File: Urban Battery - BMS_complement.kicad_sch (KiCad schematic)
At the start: 37 parts, among them J1 Conn_02x10_Odd_Even, J10 Conn_01x02_Female, J11 Conn_01x02_Female, J12 Conn_01x03, J13 Conn_01x04_Female, J2 Conn_01x02_Female, J3 Conn_01x02_Female, J4 Conn_01x02_Female, J5 Conn_01x02_Female, J6 Conn_01x03, J7 Conn_01x02_Female, J8 Conn_01x02_Female, J9 Conn_01x02_Female, K1 ADW11, K2 ADW11, SW1 Run/Charge_SW, SW2 CAN_TERM, SW3 SW_Push_LED, U1 LM2575HVS-12/NOPB, U2 MCP2515-xSO, U3 MCP2551-I-SN, Y1 8MHz

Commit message: Added temporary footprints and preliminary layout
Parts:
- removed SW1: Run/Charge_SW, symbol Switch:SW_DP3T
- added SW2: SW_DPDT_x2, BMS_Custom_Footprints:Toggle_Switch_M2022S2A2W30, symbol Switch:SW_DPDT_x2
- C1: renamed from C3; footprint (none) -> Capacitor_SMD:C_0805_2012Metric_Pad1.18x1.45mm_HandSolder
- C2: renamed from C4; footprint (none) -> Capacitor_SMD:C_0805_2012Metric_Pad1.18x1.45mm_HandSolder
- C3: renamed from C5; footprint (none) -> Capacitor_SMD:C_0805_2012Metric_Pad1.18x1.45mm_HandSolder
- C4: renamed from C6; footprint (none) -> Capacitor_SMD:C_0805_2012Metric_Pad1.18x1.45mm_HandSolder
- C6: renamed from C7; footprint (none) -> Capacitor_SMD:C_0805_2012Metric_Pad1.18x1.45mm_HandSolder
- F1: footprint (none) -> Fuse:Fuseholder_Blade_Mini_Keystone_3568
- F2: value Fuse -> 7A; footprint (none) -> Fuse:Fuseholder_Blade_Mini_Keystone_3568
- J1: value Conn_02x10_Odd_Even -> BMS IO; footprint (none) -> Connector_JST:JST_PHD_S20B-PHDSS_2x10_P2.00mm_Horizontal
- J10, J11, J9: value Conn_01x02_Female -> Thermistor; footprint (none) -> TerminalBlock_Phoenix:TerminalBlock_Phoenix_MKDS-1,5-2-5.08_1x02_P5.08mm_Horizontal
- J12: renamed from J6; value Conn_01x03 -> CAN Connector; footprint (none) -> BMS_Custom_Footprints:molex-sl-1x03-horizontal
- J13: renamed from J12; value Conn_01x03 -> CAN Connector; footprint (none) -> BMS_Custom_Footprints:molex-sl-1x03-horizontal
- J2: renamed from J13; value Conn_01x04_Female -> OLED Header; footprint (none) -> BMS_Custom_Footprints:OLED_Header
- J3, J4, J5: value Conn_01x02_Female -> E-Stop; footprint (none) -> Connector_Molex:Molex_Micro-Fit_3.0_43650-0200_1x02_P3.00mm_Horizontal
- J6: renamed from J7; value Conn_01x02_Female -> Contactor Connector; footprint (none) -> TerminalBlock_Phoenix:TerminalBlock_Phoenix_MKDS-1,5-2-5.08_1x02_P5.08mm_Horizontal
- J7: renamed from J2; value Conn_01x02_Female -> Charge Connector; footprint (none) -> Connector_Molex:Molex_Micro-Fit_3.0_43650-0200_1x02_P3.00mm_Horizontal
- J8: value Conn_01x02_Female -> Battery Connector; footprint (none) -> TerminalBlock_Phoenix:TerminalBlock_Phoenix_MKDS-1,5-2-5.08_1x02_P5.08mm_Horizontal
- K1: renamed from K2; value ADW11 -> Contactor_Relay
- K2: renamed from K1; value ADW11 -> Charge_Relay
- R1, R2, R3: footprint (none) -> Resistor_SMD:R_0805_2012Metric_Pad1.20x1.40mm_HandSolder
- Y1: footprint (none) -> Crystal:Crystal_HC49-U_Vertical
- renumbered C1 to C5, C2 to C7, SW3 to SW1, SW2 to SW3, U2 to U1, U1 to U2
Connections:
- net a2 is gone; now on net bms2: K1.6
- net a4 is gone; now on net bms4: K2.6
- net +5V: now also A1.27 (+5V), SW1.2, SW1.4 (A)
- net Buck_VIN: now also SW2.4 (A), SW2.6 (C)
- net bms2: now also SW2.1 (A)
- net bms4: now also SW2.3 (C)
- net at F1.2: now also SW2.2 (B), SW2.5 (B)
- no-connect marks 37 -> 35
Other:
- note added: "Battery Connector"
- note removed: "7A Fuse"
- note removed: "Connection to battery through bus bar pcb"
- moved on the sheet: A1, C1, C2, C3, C4, C5, C6, C7, D1, F1, F2, J1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

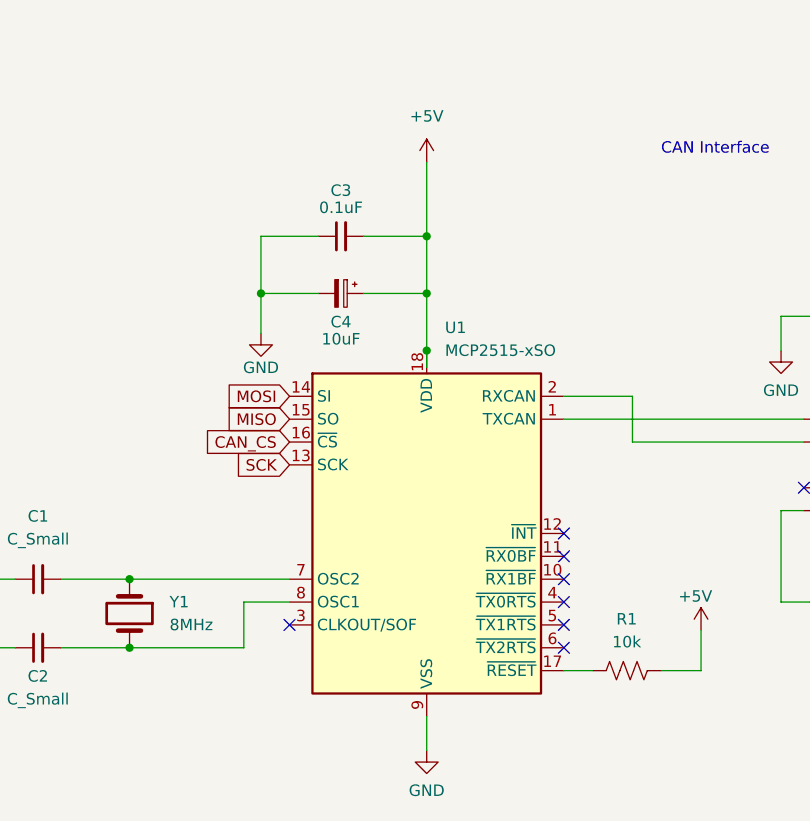
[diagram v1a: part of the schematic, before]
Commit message: Edited component placement
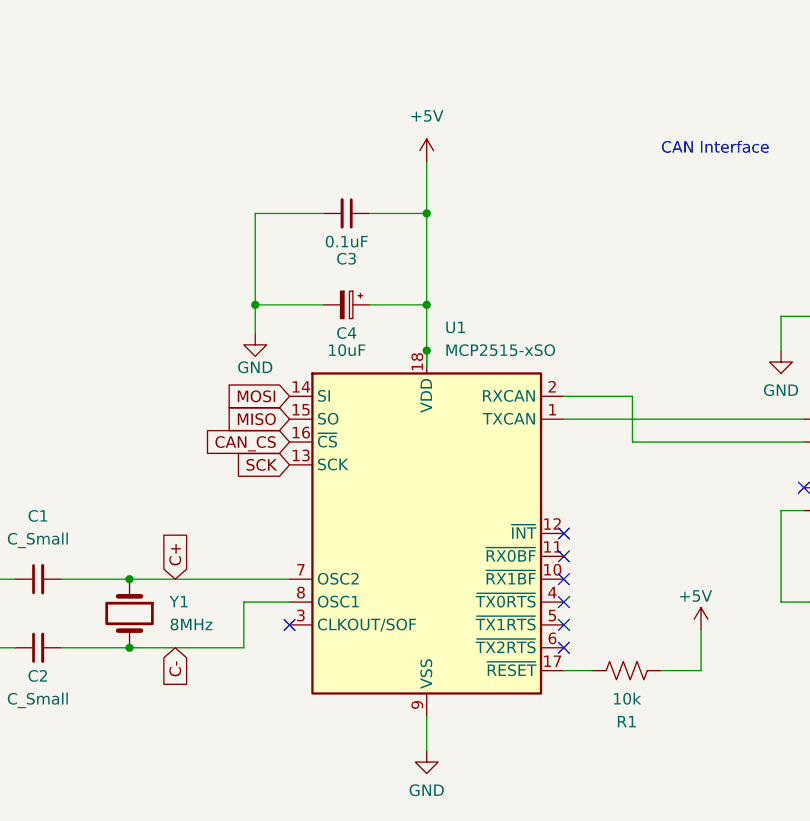
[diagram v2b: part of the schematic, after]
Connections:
- net +5V: now also C3.1, R1.1; no longer C3.2, R1.2
- net GND: now also C3.2; no longer C3.1
- net at U1.17 (~{RESET}): now also R1.2; no longer R1.1
- net C+: now reaches C1.2, U1.7 (OSC2), Y1.1
- net C-: now reaches C2.2, U1.8 (OSC1), Y1.2
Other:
- moved on the sheet: C3, C4, R1
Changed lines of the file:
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@@
   (junction (at 195.58 119.38) (diameter 0) (color 0 0 0 0)
   )
-  (junction (at 114.935 214.63) (diameter 0) (color 0 0 0 0)
-  )
   (junction (at 249.555 222.25) (diameter 0) (color 0 0 0 0)
   )
@@
   (junction (at 152.4 34.29) (diameter 0) (color 0 0 0 0)
   )
-  (junction (at 133.35 208.28) (diameter 0) (color 0 0 0 0)
-  )
   (junction (at 43.18 108.585) (diameter 0) (color 0 0 0 0)
   )
@@
   (junction (at 244.475 219.075) (diameter 0) (color 0 0 0 0)
   )
+  (junction (at 133.35 215.9) (diameter 0) (color 0 0 0 0)
+  )
   (junction (at 244.475 227.33) (diameter 0) (color 0 0 0 0)
   )
@@
   (junction (at 138.43 114.3) (diameter 0) (color 0 0 0 0)
   )
+  (junction (at 133.35 205.74) (diameter 0) (color 0 0 0 0)
+  )
   (junction (at 176.53 119.38) (diameter 0) (color 0 0 0 0)
   )
@@
   (junction (at 133.35 220.98) (diameter 0) (color 0 0 0 0)
   )
-  (junction (at 133.35 214.63) (diameter 0) (color 0 0 0 0)
-  )
   (junction (at 134.62 34.29) (diameter 0) (color 0 0 0 0)
+  )
+  (junction (at 114.3 215.9) (diameter 0) (color 0 0 0 0)
   )
   (no_connect (at 118.11 251.46))
@@
     (stroke (width 0) (type default) (color 0 0 0 0))
   )
+  (wire (pts (xy 127 205.74) (xy 133.35 205.74))
+    (stroke (width 0) (type default) (color 0 0 0 0))
+  )
   (wire (pts (xy 157.48 124.46) (xy 157.48 133.35))
     (stroke (width 0) (type default) (color 0 0 0 0))
@@
     (stroke (width 0) (type default) (color 0 0 0 0))
   )
-  (wire (pts (xy 133.35 208.28) (xy 133.35 214.63))
-    (stroke (width 0) (type default) (color 0 0 0 0))
-  )
   (wire (pts (xy 176.53 119.38) (xy 181.61 119.38))
     (stroke (width 0) (type default) (color 0 0 0 0))
@@
     (stroke (width 0) (type default) (color 0 0 0 0))
   )
-  (wire (pts (xy 121.285 208.28) (xy 114.935 208.28))
-    (stroke (width 0) (type default) (color 0 0 0 0))
-  )
   (wire (pts (xy 132.08 114.3) (xy 138.43 114.3))
     (stroke (width 0) (type default) (color 0 0 0 0))
   )
-  (wire (pts (xy 133.35 214.63) (xy 133.35 220.98))
+  (wire (pts (xy 133.35 200.025) (xy 133.35 205.74))
     (stroke (width 0) (type default) (color 0 0 0 0))
   )
@@
     (stroke (width 0) (type default) (color 0 0 0 0))
   )
+  (wire (pts (xy 114.3 215.9) (xy 114.3 219.075))
+    (stroke (width 0) (type default) (color 0 0 0 0))
+  )
   (wire (pts (xy 229.87 234.315) (xy 229.87 238.76))
     (stroke (width 0) (type default) (color 0 0 0 0))
@@
     (stroke (width 0) (type default) (color 0 0 0 0))
   )
+  (wire (pts (xy 133.35 205.74) (xy 133.35 215.9))
+    (stroke (width 0) (type default) (color 0 0 0 0))
+  )
   (wire (pts (xy 363.22 59.69) (xy 363.22 63.5))
     (stroke (width 0) (type default) (color 0 0 0 0))
@@
     (stroke (width 0) (type default) (color 0 0 0 0))
   )
-  (wire (pts (xy 133.35 200.025) (xy 133.35 208.28))
-    (stroke (width 0) (type default) (color 0 0 0 0))
-  )
-  (wire (pts (xy 126.365 214.63) (xy 133.35 214.63))
-    (stroke (width 0) (type default) (color 0 0 0 0))
-  )
   (wire (pts (xy 148.59 226.06) (xy 156.21 226.06))
     (stroke (width 0) (type default) (color 0 0 0 0))
@@
     (stroke (width 0) (type default) (color 0 0 0 0))
   )
-  (wire (pts (xy 114.935 214.63) (xy 114.935 219.075))
+  (wire (pts (xy 114.3 215.9) (xy 121.92 215.9))
     (stroke (width 0) (type default) (color 0 0 0 0))
   )
@@
     (stroke (width 0) (type default) (color 0 0 0 0))
   )
-  (wire (pts (xy 114.935 214.63) (xy 121.285 214.63))
+  (wire (pts (xy 133.35 215.9) (xy 133.35 220.98))
     (stroke (width 0) (type default) (color 0 0 0 0))
   )
@@
     (stroke (width 0) (type default) (color 0 0 0 0))
   )
-  (wire (pts (xy 126.365 208.28) (xy 133.35 208.28))
-    (stroke (width 0) (type default) (color 0 0 0 0))
-  )
   (wire (pts (xy 285.75 127) (xy 289.56 127))
     (stroke (width 0) (type default) (color 0 0 0 0))
@@
     (stroke (width 0) (type default) (color 0 0 0 0))
   )
-  (wire (pts (xy 114.935 208.28) (xy 114.935 214.63))
+  (wire (pts (xy 114.3 205.74) (xy 114.3 215.9))
     (stroke (width 0) (type default) (color 0 0 0 0))
   )
@@
     (stroke (width 0) (type default) (color 0 0 0 0))
   )
+  (wire (pts (xy 114.3 205.74) (xy 121.92 205.74))
+    (stroke (width 0) (type default) (color 0 0 0 0))
+  )
   (wire (pts (xy 163.83 252.095) (xy 163.83 256.54))
     (stroke (width 0) (type default) (color 0 0 0 0))
   )
   (wire (pts (xy 249.555 222.25) (xy 249.555 213.995))
+    (stroke (width 0) (type default) (color 0 0 0 0))
+  )
+  (wire (pts (xy 127 215.9) (xy 133.35 215.9))
     (stroke (width 0) (type default) (color 0 0 0 0))
   )
@@
     )
   )
+  (global_label "C-" (shape input) (at 105.41 254 270) (fields_autoplaced)
+    (effects (font (size 1.27 1.27)) (justify right))
+    (property "Intersheet References" "${INTERSHEET_REFS}" (id 0) (at 105.3306 259.2555 90)
+      (effects (font (size 1.27 1.27)) (justify right) hide)
+    )
+  )
+  (global_label "C+" (shape input) (at 105.41 246.38 90) (fields_autoplaced)
+    (effects (font (size 1.27 1.27)) (justify left))
+    (property "Intersheet References" "${INTERSHEET_REFS}" (id 0) (at 105.3306 241.1245 90)
+      (effects (font (size 1.27 1.27)) (justify left) hide)
+    )
+  )
   (global_label "SCK" (shape input) (at 118.11 233.68 180) (fields_autoplaced)
     (effects (font (size 1.27 1.27)) (justify right))
@@
     (pin "1")
   )
-  (symbol (lib_id "Device:C_Polarized_Small") (at 123.825 214.63 270) (unit 1)
-    (in_bom yes) (on_board yes)
-    (property "Reference" "C4" (id 0) (at 123.825 217.805 90))
-    (property "Value" "10uF" (id 1) (at 123.825 219.71 90))
-    (property "Footprint" "Capacitor_SMD:C_0805_2012Metric_Pad1.18x1.45mm_HandSolder" (id 2) (at 123.825 214.63 0)
-      (effects (font (size 1.27 1.27)) hide)
-    )
-    (property "Datasheet" "~" (id 3) (at 123.825 214.63 0)
+  (symbol (lib_id "Device:C_Polarized_Small") (at 124.46 215.9 270) (unit 1)
+    (in_bom yes) (on_board yes)
+    (property "Reference" "C4" (id 0) (at 124.46 219.075 90))
+    (property "Value" "10uF" (id 1) (at 124.46 220.98 90))
+    (property "Footprint" "Capacitor_SMD:C_0805_2012Metric_Pad1.18x1.45mm_HandSolder" (id 2) (at 124.46 215.9 0)
+      (effects (font (size 1.27 1.27)) hide)
+    )
+    (property "Datasheet" "~" (id 3) (at 124.46 215.9 0)
       (effects (font (size 1.27 1.27)) hide)
     )
@@
     (pin "4")
   )
-  (symbol (lib_id "Device:R_US") (at 155.575 256.54 90) (unit 1)
-    (in_bom yes) (on_board yes)
-    (property "Reference" "R1" (id 0) (at 155.575 250.825 90))
-    (property "Value" "10k" (id 1) (at 155.575 253.365 90))
-    (property "Footprint" "Resistor_SMD:R_0805_2012Metric_Pad1.20x1.40mm_HandSolder" (id 2) (at 155.829 255.524 90)
+  (symbol (lib_id "Device:R_US") (at 155.575 256.54 270) (unit 1)
+    (in_bom yes) (on_board yes)
+    (property "Reference" "R1" (id 0) (at 155.575 262.255 90))
+    (property "Value" "10k" (id 1) (at 155.575 259.715 90))
+    (property "Footprint" "Resistor_SMD:R_0805_2012Metric_Pad1.20x1.40mm_HandSolder" (id 2) (at 155.321 257.556 90)
       (effects (font (size 1.27 1.27)) hide)
     )
@@
     (pin "1")
   )
-  (symbol (lib_id "Device:C_Small") (at 123.825 208.28 90) (unit 1)
-    (in_bom yes) (on_board yes)
-    (property "Reference" "C3" (id 0) (at 123.825 203.2 90))
-    (property "Value" "0.1uF" (id 1) (at 123.825 205.105 90))
-    (property "Footprint" "Capacitor_SMD:C_0805_2012Metric_Pad1.18x1.45mm_HandSolder" (id 2) (at 123.825 208.28 0)
-      (effects (font (size 1.27 1.27)) hide)
-    )
-    (property "Datasheet" "~" (id 3) (at 123.825 208.28 0)
+  (symbol (lib_id "Device:C_Small") (at 124.46 205.74 270) (unit 1)
+    (in_bom yes) (on_board yes)
+    (property "Reference" "C3" (id 0) (at 124.46 210.82 90))
+    (property "Value" "0.1uF" (id 1) (at 124.46 208.915 90))
+    (property "Footprint" "Capacitor_SMD:C_0805_2012Metric_Pad1.18x1.45mm_HandSolder" (id 2) (at 124.46 205.74 0)
+      (effects (font (size 1.27 1.27)) hide)
+    )
+    (property "Datasheet" "~" (id 3) (at 124.46 205.74 0)
       (effects (font (size 1.27 1.27)) hide)
     )
@@
     (pin "2")
   )
-  (symbol (lib_id "power:GND") (at 114.935 219.075 0) (unit 1)
-    (in_bom yes) (on_board yes)
-    (property "Reference" "#PWR08" (id 0) (at 114.935 225.425 0)
-      (effects (font (size 1.27 1.27)) hide)
-    )
-    (property "Value" "GND" (id 1) (at 114.935 222.885 0))
-    (property "Footprint" "" (id 2) (at 114.935 219.075 0)
-      (effects (font (size 1.27 1.27)) hide)
-    )
-    (property "Datasheet" "" (id 3) (at 114.935 219.075 0)
-      (effects (font (size 1.27 1.27)) hide)
-    )
+  (symbol (lib_id "power:GND") (at 114.3 219.075 0) (unit 1)
+    (in_bom yes) (on_board yes)
+    (property "Reference" "#PWR08" (id 0) (at 114.3 225.425 0)
+      (effects (font (size 1.27 1.27)) hide)
+    )
+    (property "Value" "GND" (id 1) (at 114.3 222.885 0))
+    (property "Footprint" "" (id 2) (at 114.3 219.075 0)
+      (effects (font (size 1.27 1.27)) hide)
+    )
+    (property "Datasheet" "" (id 3) (at 114.3 219.075 0)
+      (effects (font (size 1.27 1.27)) hide)
+    )

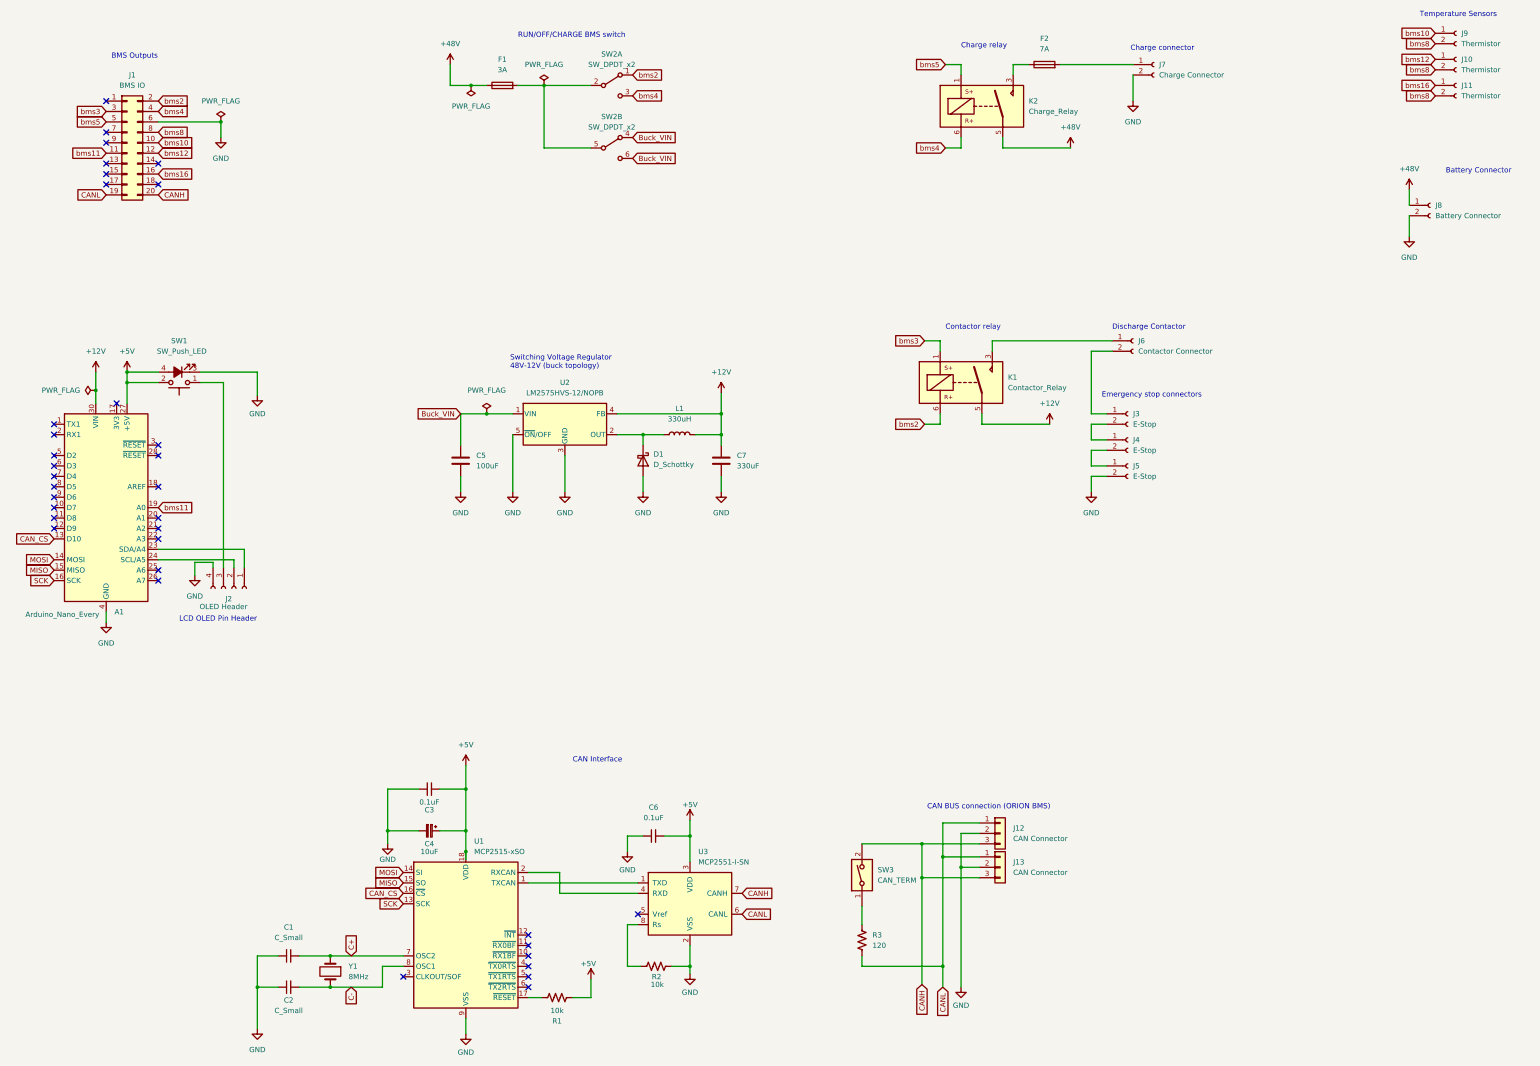
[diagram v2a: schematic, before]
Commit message: reorganized layout, started routing traces and added supermileage logo
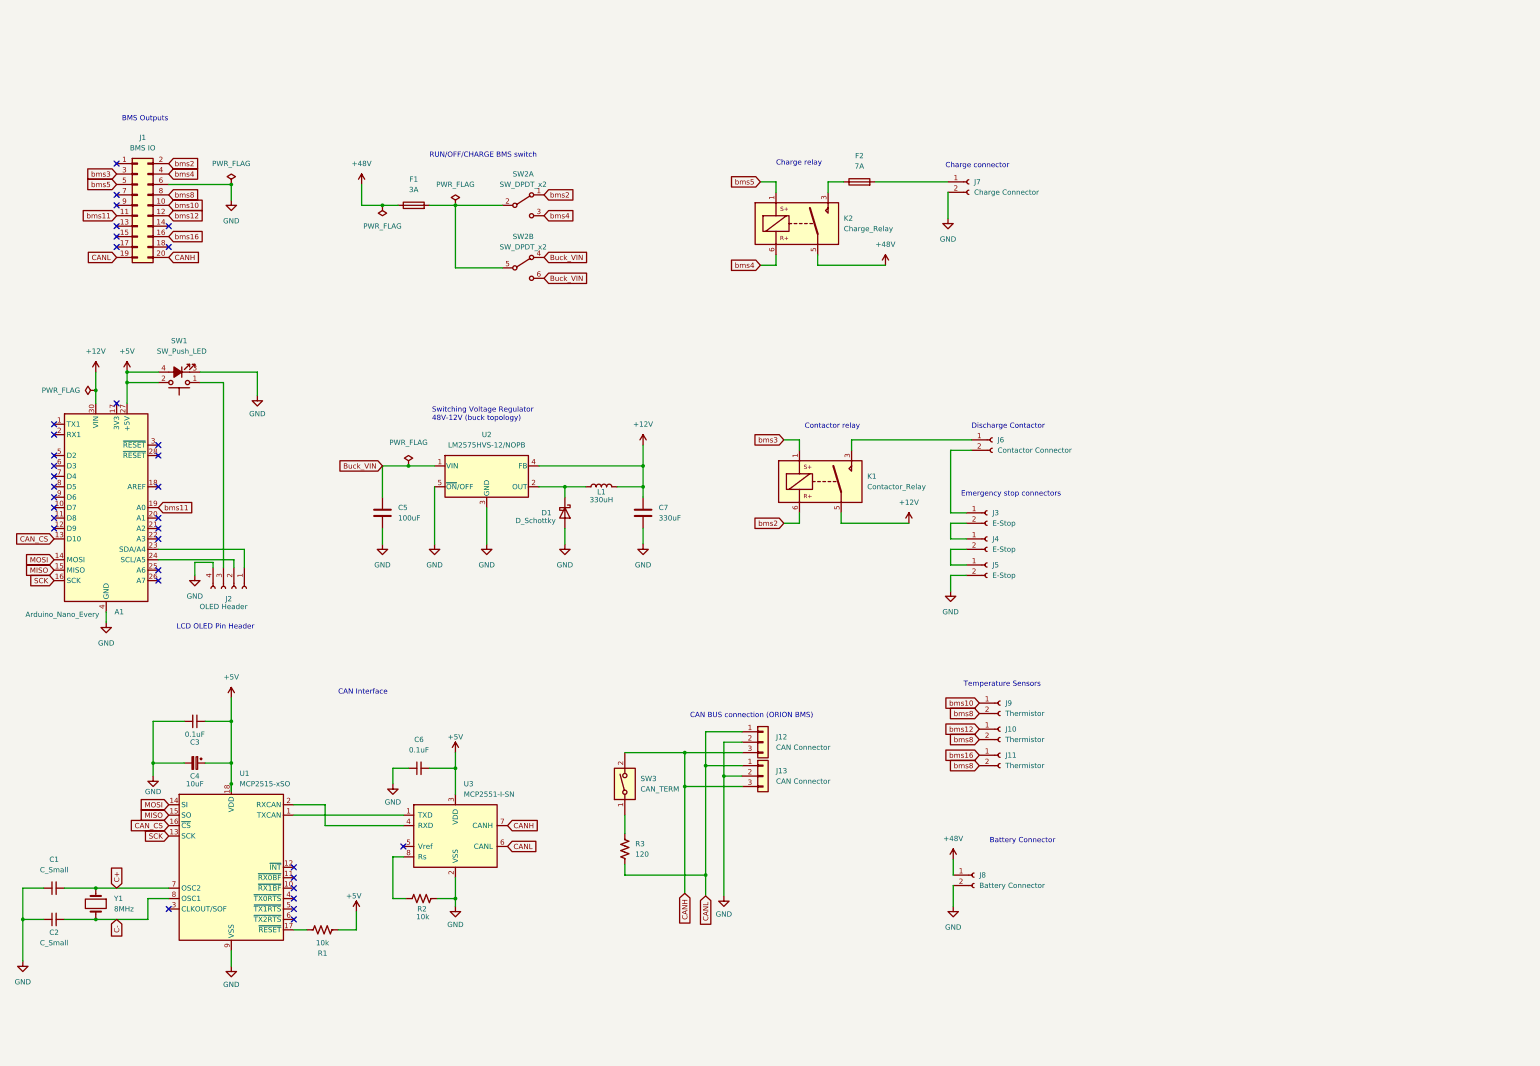
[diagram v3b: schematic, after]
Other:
- moved on the sheet: C1, C2, C3, C4, C5, C6, C7, D1, F1, F2, J1, J10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
